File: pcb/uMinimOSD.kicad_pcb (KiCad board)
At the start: 2 copper layers, 36 x 36 mm, 23 parts, among them P1 CONN_01X04, P2 CONN_01X04, P3 CONN_01X06, P4 CONN_01X06, P5 CONN_01X02

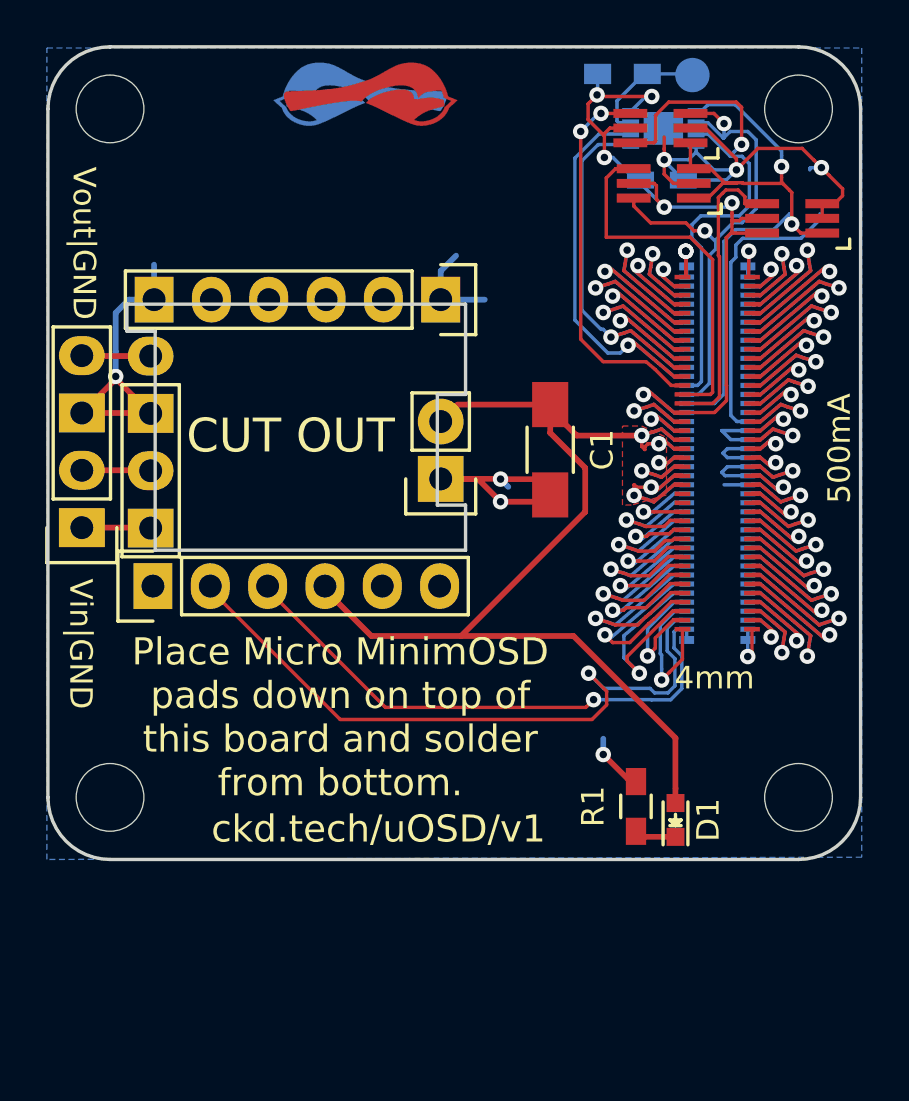
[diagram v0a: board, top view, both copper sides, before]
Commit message: v2 of uMinimOSD which corrects RX and TX and also makes it available in ftdi form.
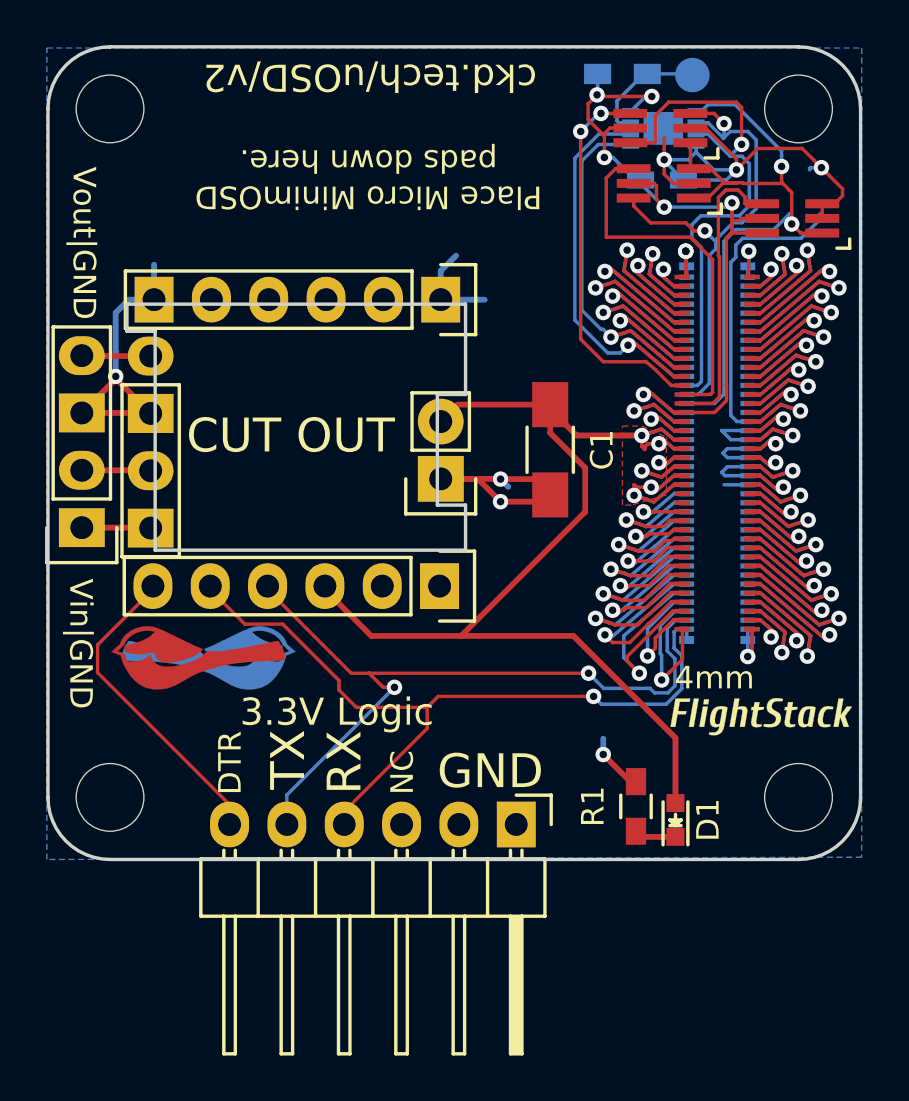
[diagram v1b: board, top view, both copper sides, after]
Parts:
- added G***: LOGO, flightstack:flightstack-8mm, F.Cu at (161.6, 119.7)
- added P6: CONN_01X06, Pin_Headers:Pin_Header_Angled_1x06, F.Cu at (150.7, 124.5)
- moved G*** 26.1 mm to (136.6, 117.1), turned to 0 degrees
- moved G*** 25.8 mm to (137.2, 117.1), turned to 180 degrees
- moved P3 12.7 mm to (147.3, 113.9), turned to 270 degrees
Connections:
- P3 pad 1: Net-(P3-Pad1) -> GNDPWR
- P3 pad 2: /ExpansionPort/UART1_TX -> GNDPWR
- P3 pad 3: /ExpansionPort/UART1_RX -> +5V
- P3 pad 4: +5V -> /ExpansionPort/UART1_TX
- P3 pad 5: GNDPWR -> /ExpansionPort/UART1_RX
- P3 pad 6: GNDPWR -> /DTR
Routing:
- net /DTR: track 0.00 -> 14.0 mm
- net /ExpansionPort/UART1_RX: track 24.6 -> 34.3 mm
- net /ExpansionPort/UART1_TX: track 29.9 -> 33.3 mm, vias 1 -> 2
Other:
- board text added: "3.3V Logic"
- board text added: "DTR"
- board text added: "GND"
- board text added: "NC"
- board text added: "Place Micro MinimOSD pads down here."
- board text added: "RX"
- board text added: "Solder from here."
- board text added: "TX"
- board text added: "ckd.tech/uOSD/v2"
- board text removed: "500mA"
- board text removed: "Place Micro MinimOSD pads down on top of this board and solder from bottom."
- board text removed: "ckd.tech/uOSD/v1"

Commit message: Correct pinout of power or IC.
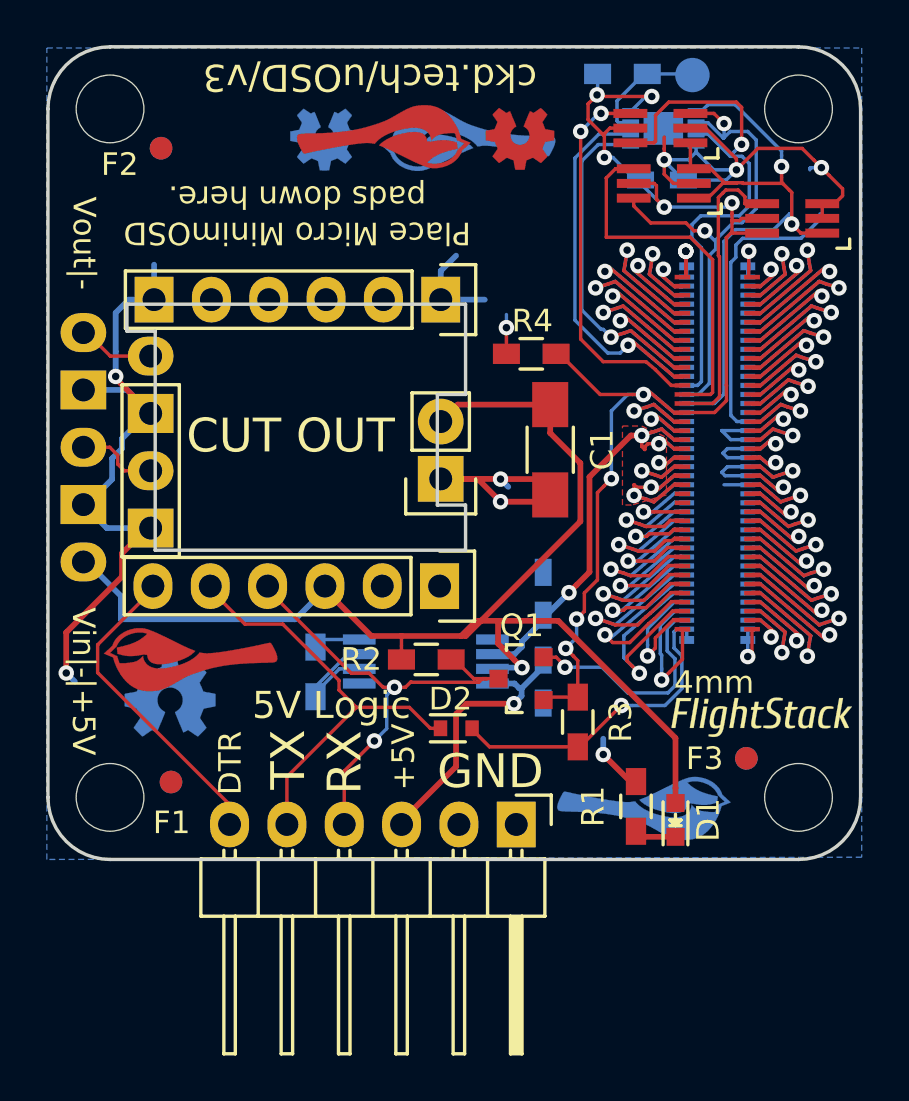
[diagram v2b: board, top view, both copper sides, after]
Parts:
- removed the G*** at (161.6, 119.7)
- added C2: 0.1uF, Capacitors_SMD:C_0603_HandSoldering, B.Cu at (151.9, 118.1)
- added C3: 0.1uF, Capacitors_SMD:C_0603_HandSoldering, B.Cu at (151.9, 114.2)
- added D2: RB751S40, Diodes_SMD:SOD-523, F.Cu at (148.1, 120.2)
- added F1: 1mm, macrofab:Fiducial, F.Cu at (135.4, 122.6)
- added F2: 1mm, macrofab:Fiducial, F.Cu at (135.0, 94.5)
- added F3: 1mm, macrofab:Fiducial, F.Cu at (160.9, 121.5)
- added F4: 1mm, macrofab:Fiducial, B.Cu at (135.4, 122.6)
- added F5: 1mm, macrofab:Fiducial, B.Cu at (135.0, 94.5)
- added F6: 1mm, macrofab:Fiducial, B.Cu at (160.9, 121.5)
- added G***: OSHW, oshw:oshw-3mm, F.Cu at (150.9, 94.1)
- added G***: Chickadee 3mm, chickadee:chickadee_3mm_fcu, F.Cu at (144.9, 94.0)
- added G***: Chickadee 3mm, chickadee:chickadee_3mm_fcu, B.Cu at (148.6, 94.1)
- added G***: LOGO, flightstack:flightstack_thin-8mm, B.Cu at (161.6, 119.7)
- added G***: LOGO, flightstack:flightstack_thin-8mm, F.Cu at (161.6, 119.7)
- added G***: OSHW, oshw:oshw-4mm, B.Cu at (135.4, 118.7)
- added G***: OSHW, oshw:oshw-3mm, B.Cu at (142.2, 94.1)
- added Q1: Q_NMOS_GSD, TO_SOT_Packages_SMD:SOT-23, F.Cu at (151.0, 118.0)
- added R2: 10k, Resistors_SMD:R_0603_HandSoldering, F.Cu at (146.8, 117.1)
- added R3: 10k, Resistors_SMD:R_0603_HandSoldering, F.Cu at (153.5, 119.9)
- added R4: 10k, Resistors_SMD:R_0603_HandSoldering, F.Cu at (151.4, 103.6)
- added R5: 470, Resistors_SMD:R_0603_HandSoldering, B.Cu at (141.8, 117.7)
- added U1: TPS2112, Housings_SSOP:TSSOP-8_4.4x3mm_Pitch0.65mm, B.Cu at (146.7, 117.2)
- C1: value C -> 10uF
- P1: value CONN_01X04 -> CONN_01X05; footprint Pin_Headers:Pin_Header_Straight_1x04 -> Pin_Headers:Pin_Header_Straight_1x05
- moved G*** 20.4 mm to (156.4, 123.7)
- moved P1 1.52 mm to (131.6, 112.8)
- moved G*** 0.35 mm to (136.3, 117.1)
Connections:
- net /ExpansionPort/3V3_0.3A_LL renamed +3V3
- P1 pad 1: GNDPWR -> +5V
- P1 pad 2: /Vin -> GNDPWR
- P1 pad 3: GNDPWR -> /Vin
- P1 pad 4: /Vout -> GNDPWR
- P3 pad 4: /ExpansionPort/UART1_TX -> /TX
- P3 pad 5: /ExpansionPort/UART1_RX -> /RX
- P6 pad 3: Net-(P6-Pad3) -> /FTDI_5V
- P6 pad 4: /ExpansionPort/UART1_RX -> /TX
- P6 pad 5: /ExpansionPort/UART1_TX -> /RX
- PORT_IN1 pad 19: +5V -> /ExpansionPort/FS_5V
- PORT_IN1 pad 20: +5V -> /ExpansionPort/FS_5V
- PORT_IN1 pad 21: +5V -> /ExpansionPort/FS_5V
- PORT_IN1 pad 22: +5V -> /ExpansionPort/FS_5V
- PORT_IN1 pad 23: +5V -> /ExpansionPort/FS_5V
- PORT_IN1 pad 24: +5V -> /ExpansionPort/FS_5V
- PORT_OUT1 pad 19: +5V -> /ExpansionPort/FS_5V
- PORT_OUT1 pad 20: +5V -> /ExpansionPort/FS_5V
- PORT_OUT1 pad 21: +5V -> /ExpansionPort/FS_5V
- PORT_OUT1 pad 22: +5V -> /ExpansionPort/FS_5V
- PORT_OUT1 pad 23: +5V -> /ExpansionPort/FS_5V
- PORT_OUT1 pad 24: +5V -> /ExpansionPort/FS_5V
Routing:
- net /ExpansionPort/FS_5V: track 0.00 -> 38.1 mm, vias 0 -> 7
- net /ExpansionPort/UART1_TX: track 33.3 -> 10.2 mm, vias 2 -> 1
- net +3V3: track 36.2 -> 57.9 mm, vias 6 -> 9
- net /TX: track 0.00 -> 21.4 mm, vias 0 -> 2
- net /RX: track 0.00 -> 20.1 mm
- net GNDPWR: track 108.8 -> 128.8 mm, vias 15 -> 17
- net /ExpansionPort/UART1_RX: track 34.3 -> 14.4 mm
- net /FTDI_5V: track 0.00 -> 12.8 mm, vias 0 -> 1
- net +5V: track 68.9 -> 58.3 mm, vias 6 -> 1
- net Net-(R5-Pad1): track 0.00 -> 2.08 mm
- net /Vin: track 3.06 -> 3.67 mm
- added copper zone on F.Cu, net /ExpansionPort/FS_5V
- removed copper zone on F.Cu, net +5V
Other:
- board text added: "+5V"
- board text added: "+5V|-|Vin"
- board text added: "-|Vout"
- board text added: "5V Logic"
- board text added: "Vin|-|+5V"
- board text added: "Vout|-"
- board text added: "ckd.tech/uOSD/v3"
- board text removed: "3.3V Logic"
- board text removed: "GND|Vin"
- board text removed: "GND|Vout"
- board text removed: "NC"
- board text removed: "Vin|GND"
- board text removed: "Vout|GND"
- board text removed: "ckd.tech/uOSD/v2"

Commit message: Rebrand everything to Polystack and increment versions.
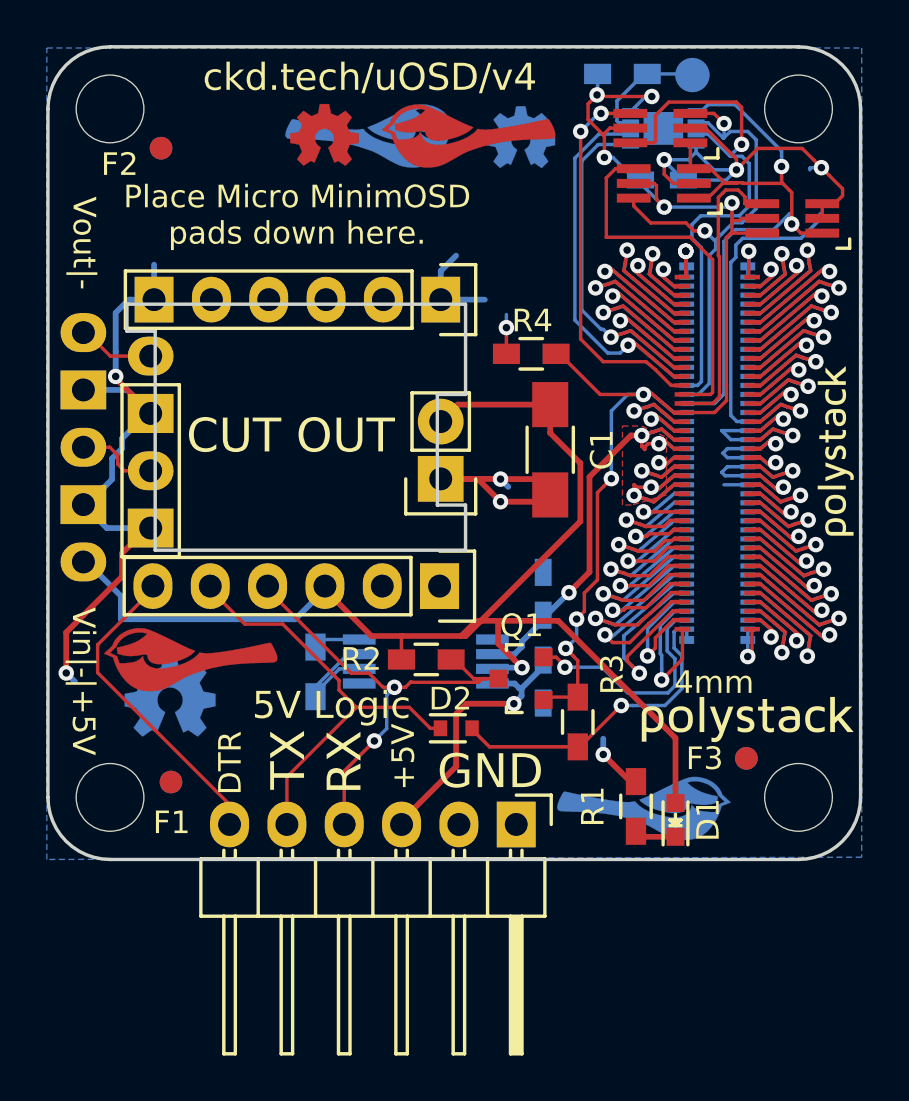
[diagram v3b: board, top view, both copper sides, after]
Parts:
- removed the G*** at (161.6, 119.7) (x2)
- added svg2mod: G***, polystack:polystack-medium-0.4, B.Cu at (164.9, 107.9)
- added svg2mod: G***, polystack:polystack-medium-0.5, B.Cu at (160.9, 119.8)
- added svg2mod: G***, polystack:polystack-medium-0.5, F.Cu at (161.0, 119.8)
- added svg2mod: G***, polystack:polystack-medium-0.4, F.Cu at (164.9, 107.9)
- moved G*** 8.70 mm to (150.9, 94.0), turned to 180 degrees
- moved G*** 8.66 mm to (142.2, 93.9), turned to 0 degrees
- moved G*** 4.20 mm to (144.4, 94.0), turned to 180 degrees
- moved G*** 3.69 mm to (148.6, 94.0), turned to 0 degrees
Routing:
- net GNDPWR: track 128.8 -> 127.8 mm
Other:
- rule pad_to_mask_clearance: 0.2 -> 0.0762
- board text added: "ckd.tech/uOSD/v4"
- board text removed: "ckd.tech/uOSD/v3"
